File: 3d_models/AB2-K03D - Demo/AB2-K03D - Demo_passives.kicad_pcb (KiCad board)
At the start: 2 copper layers, 22 parts

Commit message: AB2-K03D: add 0805 LED RED/YEL/GRN/BLU
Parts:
- added AB2_0805_LED_BLU: VAL**, AB2_0805_LED_BLU, F.Cu at (182.9, 129.5)
- added AB2_0805_LED_GRN: VAL**, AB2_0805_LED_GRN, F.Cu at (180.3, 129.5)
- added AB2_0805_LED_RED: VAL**, AB2_0805_LED_RED, F.Cu at (175.3, 129.5)
- added AB2_0805_LED_YEL: VAL**, AB2_0805_LED_YEL, F.Cu at (177.8, 129.5)
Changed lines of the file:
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@@
     (links 0)
     (no_connects 0)
-    (area 8.1915 110.593012 302.9585 286.4485)
+    (area 173.2915 106.783012 216.5985 152.663877)
     (thickness 1.6)
     (drawings 0)
     (tracks 0)
     (zones 0)
-    (modules 22)
+    (modules 26)
     (nets 1)
   )
@@
       (at (xyz 0 0 0))
       (scale (xyz 0.3937 0.3937 0.3937))
+      (rotate (xyz 0 0 0))
+    )
+  )
+  (module AB2_0805_LED_YEL (layer F.Cu)
+    (at 177.8 129.54 270)
+    (fp_text reference AB2_0805_LED_YEL (at 0 -1.27 270) (layer F.SilkS)
+      (effects (font (size 0.8128 0.8128) (thickness 0.0762)))
+    )
+    (fp_text value VAL** (at 0 1.27 270) (layer F.SilkS)
+      (effects (font (size 0.8128 0.8128) (thickness 0.0762)))
+    )
+    (fp_line (start 0.254 -0.127) (end 0.254 0.127) (layer F.SilkS) (width 0.127))
+    (fp_line (start 0.381 0) (end 0 0.254) (layer F.SilkS) (width 0.127))
+    (fp_line (start 0.381 0) (end 0 -0.254) (layer F.SilkS) (width 0.127))
+    (fp_line (start 0.127 -0.254) (end 0.127 0.254) (layer F.SilkS) (width 0.127))
+    (fp_line (start 0 -0.381) (end 0 0.381) (layer F.SilkS) (width 0.127))
+    (fp_line (start 0 0.381) (end 0.508 0) (layer F.SilkS) (width 0.127))
+    (fp_line (start 0.508 0) (end 0 -0.381) (layer F.SilkS) (width 0.127))
+    (fp_line (start 0.85 0.6) (end 0.85 -0.6) (layer F.SilkS) (width 0.127))
+    (fp_line (start 0.75 -0.6) (end 0.75 0.6) (layer F.SilkS) (width 0.127))
+    (fp_line (start -0.85 0.6) (end -0.85 -0.6) (layer F.SilkS) (width 0.127))
+    (fp_line (start -0.75 -0.6) (end -0.75 0.6) (layer F.SilkS) (width 0.127))
+    (fp_line (start -0.95 -0.6) (end 0.95 -0.6) (layer F.SilkS) (width 0.127))
+    (fp_line (start 0.95 -0.6) (end 0.95 0.6) (layer F.SilkS) (width 0.127))
+    (fp_line (start 0.95 0.6) (end -0.95 0.6) (layer F.SilkS) (width 0.127))
+    (fp_line (start -0.95 0.6) (end -0.95 -0.6) (layer F.SilkS) (width 0.127))
+    (pad 1 smd rect (at -1.1 0 270) (size 0.9 1.3)
+      (layers F.Cu F.Paste F.Mask)
+    )
+    (pad 2 smd rect (at 1.1 0 270) (size 0.9 1.3)
+      (layers F.Cu F.Paste F.Mask)
+    )
+    (model ../3d_models/ab2_passive/AB2_0805_LED_YEL.wrl
+      (at (xyz 0 0 0))
+      (scale (xyz 0.3937 0.3937 0.3937))
+      (rotate (xyz 0 0 0))
+    )
+  )
+  (module AB2_0805_LED_RED (layer F.Cu)
+    (at 175.26 129.54 270)
+    (fp_text reference AB2_0805_LED_RED (at 0 -1.27 270) (layer F.SilkS)
+      (effects (font (size 0.8128 0.8128) (thickness 0.0762)))
+    )
+    (fp_text value VAL** (at 0 1.27 270) (layer F.SilkS)
+      (effects (font (size 0.8128 0.8128) (thickness 0.0762)))
+    )
+    (fp_line (start 0.254 -0.127) (end 0.254 0.127) (layer F.SilkS) (width 0.127))
+    (fp_line (start 0.381 0) (end 0 0.254) (layer F.SilkS) (width 0.127))
+    (fp_line (start 0.381 0) (end 0 -0.254) (layer F.SilkS) (width 0.127))
+    (fp_line (start 0.127 -0.254) (end 0.127 0.254) (layer F.SilkS) (width 0.127))
+    (fp_line (start 0 -0.381) (end 0 0.381) (layer F.SilkS) (width 0.127))
+    (fp_line (start 0 0.381) (end 0.508 0) (layer F.SilkS) (width 0.127))
+    (fp_line (start 0.508 0) (end 0 -0.381) (layer F.SilkS) (width 0.127))
+    (fp_line (start 0.85 0.6) (end 0.85 -0.6) (layer F.SilkS) (width 0.127))
+    (fp_line (start 0.75 -0.6) (end 0.75 0.6) (layer F.SilkS) (width 0.127))
+    (fp_line (start -0.85 0.6) (end -0.85 -0.6) (layer F.SilkS) (width 0.127))
+    (fp_line (start -0.75 -0.6) (end -0.75 0.6) (layer F.SilkS) (width 0.127))
+    (fp_line (start -0.95 -0.6) (end 0.95 -0.6) (layer F.SilkS) (width 0.127))
+    (fp_line (start 0.95 -0.6) (end 0.95 0.6) (layer F.SilkS) (width 0.127))
+    (fp_line (start 0.95 0.6) (end -0.95 0.6) (layer F.SilkS) (width 0.127))
+    (fp_line (start -0.95 0.6) (end -0.95 -0.6) (layer F.SilkS) (width 0.127))
+    (pad 1 smd rect (at -1.1 0 270) (size 0.9 1.3)
+      (layers F.Cu F.Paste F.Mask)
+    )
+    (pad 2 smd rect (at 1.1 0 270) (size 0.9 1.3)
+      (layers F.Cu F.Paste F.Mask)
+    )
+    (model ../3d_models/ab2_passive/AB2_0805_LED_RED.wrl
+      (at (xyz 0 0 0))
+      (scale (xyz 0.3937 0.3937 0.3937))
+      (rotate (xyz 0 0 0))
+    )
+  )
+  (module AB2_0805_LED_GRN (layer F.Cu)
+    (at 180.34 129.54 270)
+    (fp_text reference AB2_0805_LED_GRN (at 0 -1.27 270) (layer F.SilkS)
+      (effects (font (size 0.8128 0.8128) (thickness 0.0762)))
+    )
+    (fp_text value VAL** (at 0 1.27 270) (layer F.SilkS)
+      (effects (font (size 0.8128 0.8128) (thickness 0.0762)))
+    )
+    (fp_line (start 0.254 -0.127) (end 0.254 0.127) (layer F.SilkS) (width 0.127))
+    (fp_line (start 0.381 0) (end 0 0.254) (layer F.SilkS) (width 0.127))
+    (fp_line (start 0.381 0) (end 0 -0.254) (layer F.SilkS) (width 0.127))
+    (fp_line (start 0.127 -0.254) (end 0.127 0.254) (layer F.SilkS) (width 0.127))
+    (fp_line (start 0 -0.381) (end 0 0.381) (layer F.SilkS) (width 0.127))
+    (fp_line (start 0 0.381) (end 0.508 0) (layer F.SilkS) (width 0.127))
+    (fp_line (start 0.508 0) (end 0 -0.381) (layer F.SilkS) (width 0.127))
+    (fp_line (start 0.85 0.6) (end 0.85 -0.6) (layer F.SilkS) (width 0.127))
+    (fp_line (start 0.75 -0.6) (end 0.75 0.6) (layer F.SilkS) (width 0.127))
+    (fp_line (start -0.85 0.6) (end -0.85 -0.6) (layer F.SilkS) (width 0.127))
+    (fp_line (start -0.75 -0.6) (end -0.75 0.6) (layer F.SilkS) (width 0.127))
+    (fp_line (start -0.95 -0.6) (end 0.95 -0.6) (layer F.SilkS) (width 0.127))
+    (fp_line (start 0.95 -0.6) (end 0.95 0.6) (layer F.SilkS) (width 0.127))
+    (fp_line (start 0.95 0.6) (end -0.95 0.6) (layer F.SilkS) (width 0.127))
+    (fp_line (start -0.95 0.6) (end -0.95 -0.6) (layer F.SilkS) (width 0.127))
+    (pad 1 smd rect (at -1.1 0 270) (size 0.9 1.3)
+      (layers F.Cu F.Paste F.Mask)
+    )
+    (pad 2 smd rect (at 1.1 0 270) (size 0.9 1.3)
+      (layers F.Cu F.Paste F.Mask)
+    )
+    (model ../3d_models/ab2_passive/AB2_0805_LED_GRN.wrl
+      (at (xyz 0 0 0))
+      (scale (xyz 0.3937 0.3937 0.3937))
+      (rotate (xyz 0 0 0))
+    )
+  )
+  (module AB2_0805_LED_BLU (layer F.Cu)
+    (at 182.88 129.54 270)
+    (fp_text reference AB2_0805_LED_BLU (at 0 -1.27 270) (layer F.SilkS)
+      (effects (font (size 0.8128 0.8128) (thickness 0.0762)))
+    )
+    (fp_text value VAL** (at 0 1.27 270) (layer F.SilkS)
+      (effects (font (size 0.8128 0.8128) (thickness 0.0762)))
+    )
+    (fp_line (start 0.254 -0.127) (end 0.254 0.127) (layer F.SilkS) (width 0.127))
+    (fp_line (start 0.381 0) (end 0 0.254) (layer F.SilkS) (width 0.127))
+    (fp_line (start 0.381 0) (end 0 -0.254) (layer F.SilkS) (width 0.127))
+    (fp_line (start 0.127 -0.254) (end 0.127 0.254) (layer F.SilkS) (width 0.127))
+    (fp_line (start 0 -0.381) (end 0 0.381) (layer F.SilkS) (width 0.127))
+    (fp_line (start 0 0.381) (end 0.508 0) (layer F.SilkS) (width 0.127))
+    (fp_line (start 0.508 0) (end 0 -0.381) (layer F.SilkS) (width 0.127))
+    (fp_line (start 0.85 0.6) (end 0.85 -0.6) (layer F.SilkS) (width 0.127))
+    (fp_line (start 0.75 -0.6) (end 0.75 0.6) (layer F.SilkS) (width 0.127))
+    (fp_line (start -0.85 0.6) (end -0.85 -0.6) (layer F.SilkS) (width 0.127))
+    (fp_line (start -0.75 -0.6) (end -0.75 0.6) (layer F.SilkS) (width 0.127))
+    (fp_line (start -0.95 -0.6) (end 0.95 -0.6) (layer F.SilkS) (width 0.127))
+    (fp_line (start 0.95 -0.6) (end 0.95 0.6) (layer F.SilkS) (width 0.127))
+    (fp_line (start 0.95 0.6) (end -0.95 0.6) (layer F.SilkS) (width 0.127))
+    (fp_line (start -0.95 0.6) (end -0.95 -0.6) (layer F.SilkS) (width 0.127))
+    (pad 1 smd rect (at -1.1 0 270) (size 0.9 1.3)
+      (layers F.Cu F.Paste F.Mask)
+    )
+    (pad 2 smd rect (at 1.1 0 270) (size 0.9 1.3)
+      (layers F.Cu F.Paste F.Mask)
+    )
+    (model ../3d_models/ab2_passive/AB2_0805_LED_BLU.wrl
+      (at (xyz 0 0 0))
+      (scale (xyz 0.3937 0.3937 0.3937))

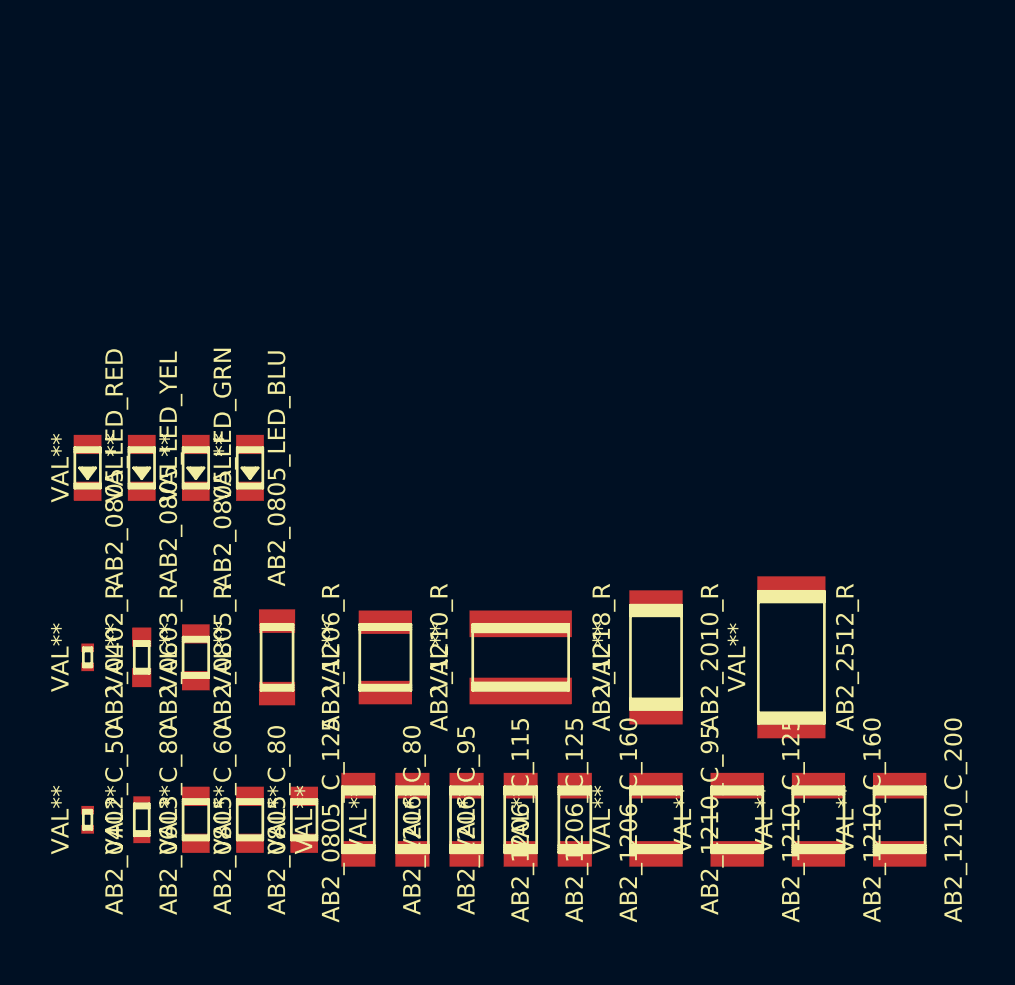
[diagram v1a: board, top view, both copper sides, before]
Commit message: AB2-K03D: add 5050 (PLCC6) RGB LEDs to passive
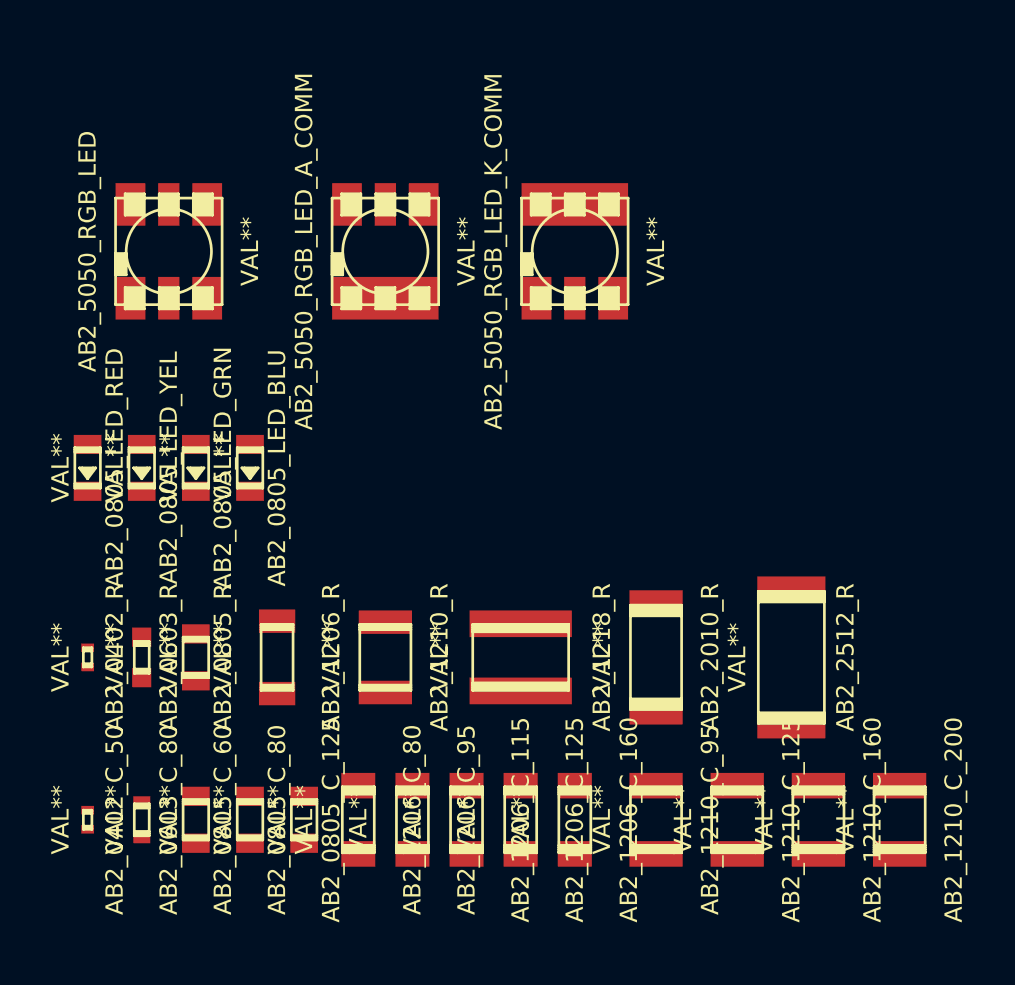
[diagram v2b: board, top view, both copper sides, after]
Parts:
- added AB2_5050_RGB_LED: VAL**, AB2_5050_RGB_LED, F.Cu at (179.1, 119.4)
- added AB2_5050_RGB_LED_A_COMM: VAL**, AB2_5050_RGB_LED_A_COMM, F.Cu at (189.2, 119.4)
- added AB2_5050_RGB_LED_K_COMM: VAL**, AB2_5050_RGB_LED_K_COMM, F.Cu at (198.1, 119.4)
